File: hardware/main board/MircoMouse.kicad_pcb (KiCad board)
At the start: 8 copper layers, 50 x 50 mm, 74 parts, among them IC1 STM32WB55RGV6, IC2 DRV8212PDSGR, IC3 DRV8212PDSGR, IC4 W25N01GVZEIG, IC5 LSM6DSLTR, IC6 SN74LVC1G18DBVRG4, IC7 SN74LVC1G18DBVRG4, J1 JST-SH 01x06, J2 JST-SH 01x06, J3 JST_XH_B3B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

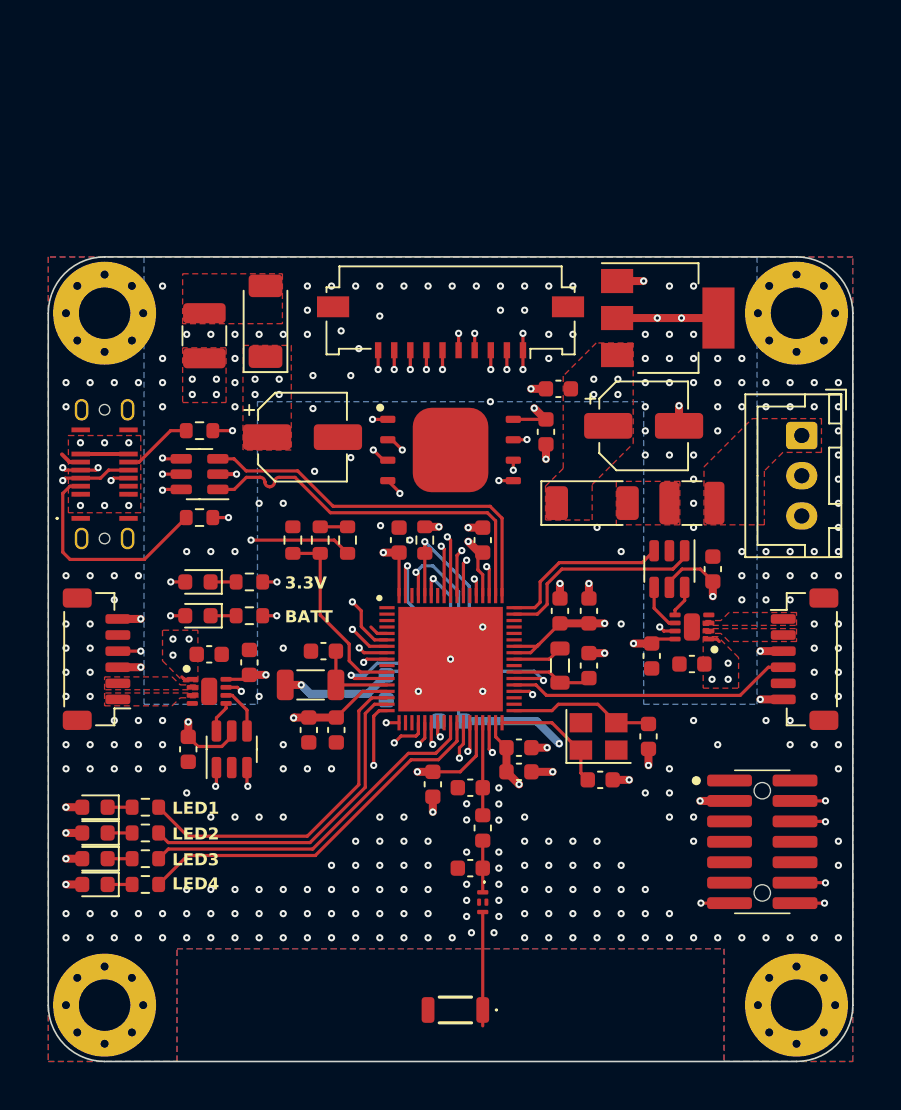
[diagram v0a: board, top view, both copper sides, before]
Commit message: schematic changes to change it into a micro mouse
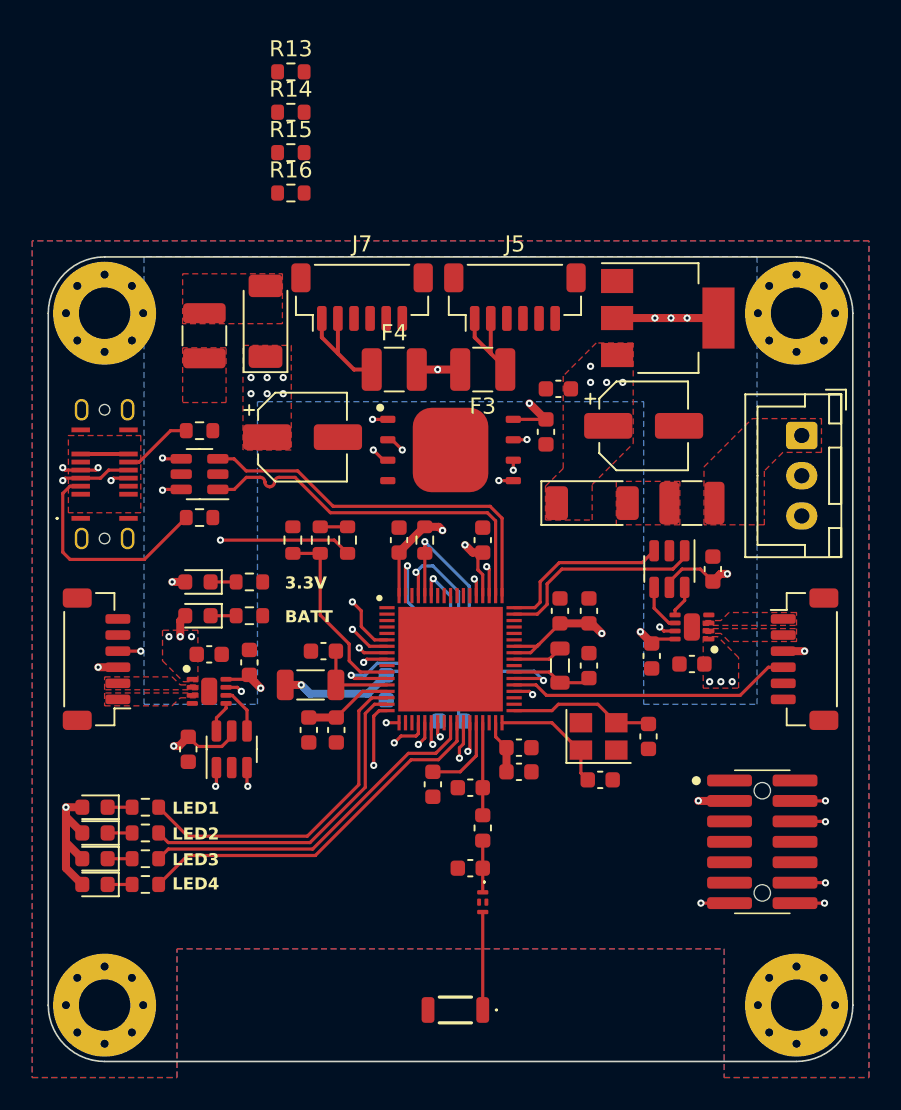
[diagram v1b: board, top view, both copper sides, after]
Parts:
- added F3: 0.5A/16V, Fuse:Fuse_1210_3225Metric, F.Cu at (149.0, 46.0)
- added F4: 0.5A/16V, Fuse:Fuse_1210_3225Metric, F.Cu at (143.5, 46.0)
- added J5: JST-SH 01x06, Connector_JST:JST_SH_BM06B-SRSS-TB_1x06-1MP_P1.00mm_Vertical, F.Cu at (151.0, 41.5)
- added R13: 100, Resistor_SMD:R_0603_1608Metric, F.Cu at (137.1, 27.5)
- added R14: 100, Resistor_SMD:R_0603_1608Metric, F.Cu at (137.1, 30.0)
- added R15: 100, Resistor_SMD:R_0603_1608Metric, F.Cu at (137.1, 32.5)
- added R16: 100, Resistor_SMD:R_0603_1608Metric, F.Cu at (137.1, 35.0)
- C1, C2: value 20pF -> 30pF
- J7: value Conn_01x10 -> JST-SH 01x06; footprint Connector_FFC-FPC:Molex_200528-0100_1x10-1MP_P1.00mm_Horizontal -> Connector_JST:JST_SH_BM06B-SRSS-TB_1x06-1MP_P1.00mm_Vertical
- Y1: value X322516MLB4SI -> 8MHz
- moved J7 6.00 mm to (141.5, 41.5), turned to 0 degrees
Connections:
- net /M_LEFT+ renamed /Motor Control Left/M+
- net /M_LEFT- renamed /Motor Control Left/M-
- net /M_RIGHT+ renamed /Motor Control Right/M+
- net /M_RIGHT- renamed /Motor Control Right/M-
- IC1 pad 10: unconnected-(IC1A-PC1-Pad10) -> /uC/WALL_DETECT_F
- IC1 pad 19: unconnected-(IC1A-PA4-Pad19) -> /uC/WALL_DETECT_R
- IC1 pad 20: unconnected-(IC1A-PA5-Pad20) -> /uC/WALL_DETECT_B
- IC1 pad 25: unconnected-(IC1A-PC4-Pad25) -> /uC/WALL_DETECT_L
- IC1 pad 58: /~{SPI_EX1_CS} -> unconnected-(IC1A-PC10-Pad58)
- IC1 pad 59: /~{SPI_EX2_CS} -> unconnected-(IC1A-PC11-Pad59)
- IC1 pad 60: /SPI_EX_INT1 -> unconnected-(IC1A-PC12-Pad60)
- IC1 pad 61: /SPI_EX_INT2 -> unconnected-(IC1A-PD0-Pad61)
- IC1 pad 63: /SPI_CLK -> /uC/SPI_CLK
- IC1 pad 64: /SPI_MISO -> /uC/SPI_MISO
- IC1 pad 65: /SPI_MOSI -> /uC/SPI_MOSI
- IC5 pad 1: /SPI_MISO -> /uC/SPI_MISO
- IC5 pad 13: /SPI_CLK -> /uC/SPI_CLK
- IC5 pad 14: /SPI_MOSI -> /uC/SPI_MOSI
- J1 pad 5: unconnected-(J1-Pin_5-Pad5) -> /M_RIGHT_B
- J2 pad 5: unconnected-(J2-Pin_5-Pad5) -> /M_LEFT_B
- J7 pad 1: GND -> Net-(J7-Pin_1)
- J7 pad 2: /SPI_MISO -> Net-(J7-Pin_1)
- J7 pad 3: /SPI_MOSI -> Net-(J7-Pin_3)
- J7 pad 4: GND -> Net-(J7-Pin_4)
- J7 pad 5: /SPI_CLK -> GND
- J7 pad 6: /~{SPI_EX1_CS} -> GND
- J7 pad MP: GND -> (no net)
- R1 pad 2: /SPI_MISO -> /uC/SPI_MISO
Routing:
- net /SPI_MISO: track 50.6 -> 0.00 mm, vias 2 -> 0
- net /SPI_MOSI: track 47.3 -> 0.00 mm, vias 2 -> 0
- net /SPI_CLK: track 44.4 -> 0.00 mm, vias 2 -> 0
- net GND: track 30.7 -> 0.00 mm, vias 305 -> 0
- net /~{SPI_EX1_CS}: track 16.6 -> 0.00 mm, vias 2 -> 0
- net /SPI_EX_INT2: track 16.6 -> 0.00 mm, vias 2 -> 0
- net /SPI_EX_INT1: track 16.3 -> 0.00 mm, vias 2 -> 0
- net /~{SPI_EX2_CS}: track 16.3 -> 0.00 mm, vias 2 -> 0
- net /uC/SPI_MOSI: track 0.00 -> 14.9 mm, vias 0 -> 1
- net /uC/SPI_MISO: track 0.00 -> 11.8 mm, vias 0 -> 1
- net Net-(J7-Pin_1): track 0.00 -> 7.28 mm
- net Net-(J5-Pin_1): track 0.00 -> 6.14 mm
- net /uC/SPI_CLK: track 0.00 -> 5.64 mm, vias 0 -> 1
- net /VBUS: track 5.79 -> 2.97 mm, vias 11 -> 0
- net +3.3V: track 88.3 -> 87.1 mm, vias 25 -> 18
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
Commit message: done
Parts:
- R13, R14, R15, R16: moved to B.Cu
- moved R13 34.9 mm to (155.8, 57.0), turned to -90 degrees
- moved R14 33.7 mm to (157.2, 57.0), turned to -90 degrees
- moved R15 29.1 mm to (152.8, 57.0), turned to -90 degrees
- moved R16 27.9 mm to (154.2, 57.0), turned to -90 degrees
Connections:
- IC1 pad 10: /uC/WALL_DETECT_F -> unconnected-(IC1A-PC1-Pad10)
- IC1 pad 19: /uC/WALL_DETECT_R -> unconnected-(IC1A-PA4-Pad19)
- IC1 pad 20: /uC/WALL_DETECT_B -> unconnected-(IC1A-PA5-Pad20)
- IC1 pad 25: /uC/WALL_DETECT_L -> unconnected-(IC1A-PC4-Pad25)
- IC1 pad 58: unconnected-(IC1A-PC10-Pad58) -> /WALL_DETECT_R
- IC1 pad 59: unconnected-(IC1A-PC11-Pad59) -> /WALL_DETECT_F
- IC1 pad 60: unconnected-(IC1A-PC12-Pad60) -> /WALL_DETECT_L
- IC1 pad 61: unconnected-(IC1A-PD0-Pad61) -> /WALL_DETECT_B
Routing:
- net Net-(J7-Pin_4): track 0.00 -> 23.9 mm, vias 0 -> 2
- net Net-(J7-Pin_3): track 0.00 -> 23.5 mm, vias 0 -> 2
- net Net-(J5-Pin_4): track 0.00 -> 17.4 mm, vias 0 -> 2
- net Net-(J5-Pin_3): track 0.00 -> 17.2 mm, vias 0 -> 2
- net /WALL_DETECT_R: track 0.00 -> 13.6 mm, vias 0 -> 1
- net /WALL_DETECT_L: track 0.00 -> 13.3 mm, vias 0 -> 1
- net /WALL_DETECT_B: track 0.00 -> 12.9 mm, vias 0 -> 1
- net /WALL_DETECT_F: track 0.00 -> 12.9 mm, vias 0 -> 1
- net +3.3V: track 87.1 -> 94.3 mm, vias 18 -> 21
- net GND: track 0.00 -> 2.57 mm, vias 0 -> 122
- net /VBUS: track 2.97 -> 4.13 mm, vias 0 -> 9

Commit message: final
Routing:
- net /uC/QSPI_IO0: track 28.8 -> 31.0 mm
- net /uC/QSPI_CLK: track 28.9 -> 31.0 mm
- net /uC/QSPI_IO3: track 29.0 -> 31.1 mm
- net /uC/QSPI_IO2: track 29.0 -> 31.2 mm
- net /uC/QSPI_IO1: track 28.9 -> 31.0 mm
